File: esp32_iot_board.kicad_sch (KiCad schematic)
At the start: 25 parts, among them J1 SS-52400-002, J2 B2B-PH-SM4-TB, U1 MCP73871

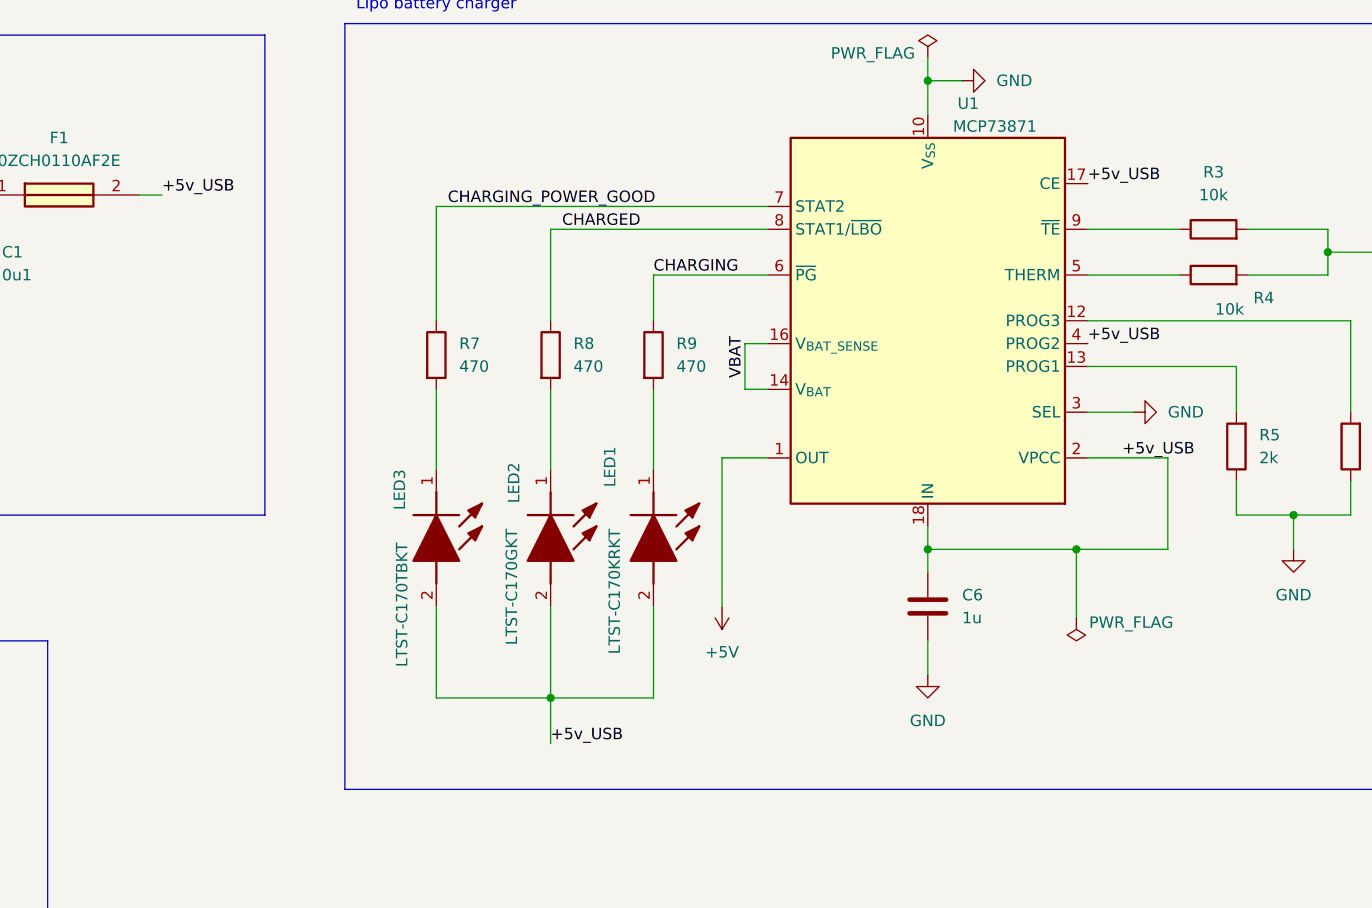
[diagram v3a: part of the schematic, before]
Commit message: refactor: update label naming for net class scope resolution; set up PCB constraints
- Renamed schematic labels to follow a net class–based naming convention for
better scope resolution (e.g., labels in the SPI net class now use a SPI_ prefix).

- Configured the PCB stack-up to use a 4-layer board.

- Applied design constraints (e.g., trace width, spacing) based on the
PCB manufacturer's recommended specifications.
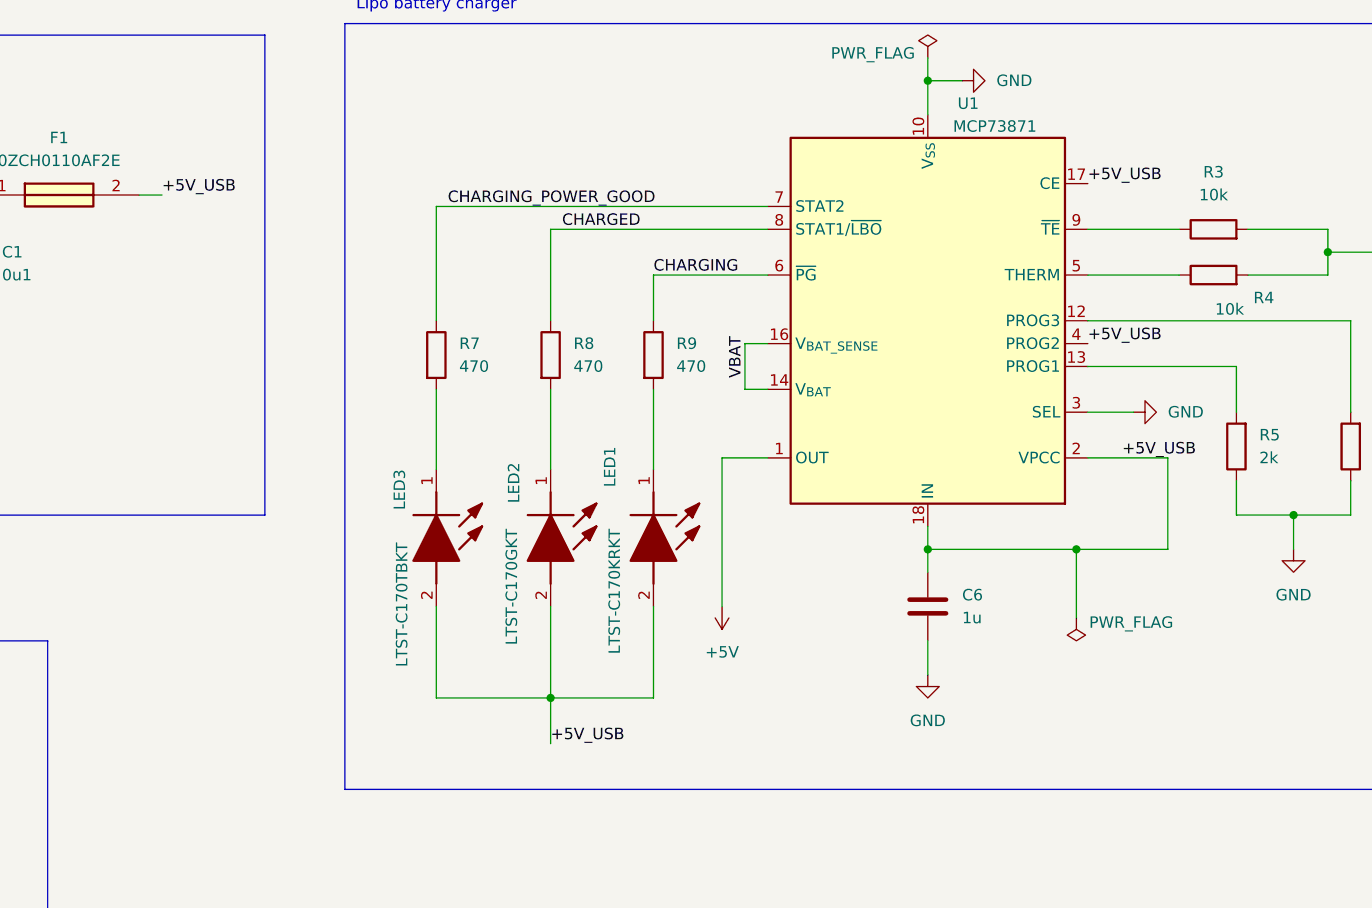
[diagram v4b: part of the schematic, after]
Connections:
- net +5v_USB renamed +5V_USB
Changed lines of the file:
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@@
 		)
 	)
-	(label "+5v_USB"
+	(label "+5V_USB"
 		(at 226.06 38.1 0)
 		(effects
@@
 		)
 	)
-	(label "+5v_USB"
+	(label "+5V_USB"
 		(at 166.37 100.33 0)
 		(effects
@@
 		)
 	)
-	(label "+5v_USB"
+	(label "+5V_USB"
 		(at 229.87 68.58 0)
 		(effects
@@
 		)
 	)
-	(label "+5v_USB"
+	(label "+5V_USB"
 		(at 226.06 55.88 0)
 		(effects
@@
 		)
 	)
-	(label "+5v_USB"
+	(label "+5V_USB"
 		(at 123.19 39.37 0)
 		(effects
